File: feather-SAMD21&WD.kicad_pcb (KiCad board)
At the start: 2 copper layers, 50.8 x 22.9 mm, 35 parts, among them J1 JumperSET0, J2 JumperSET1, J3 JumperSET2, J4 left_header, J5 right_header, J6 Batt_header, J7 reset_enable, J8 16P_USB_C, SW1 SW_Push, U1 MAX6369, U2 USBLC6-2SC6, U3 ATSAMD21G18A-M, X1 32.768

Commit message: rev one, routing done
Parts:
- moved R5 8.13 mm to (140.4, 88.4)
- moved SW1 1.50 mm to (138.4, 86.6)
- moved C2 1.46 mm to (146.0, 85.0)
- moved C1 0.89 mm to (140.4, 92.4), turned to 180 degrees
- moved R4 0.89 mm to (140.4, 90.4), turned to 180 degrees
- moved U1 0.59 mm to (145.9, 88.2)
- moved C4 0.54 mm to (136.8, 86.4)
- moved U2 0.52 mm to (117.4, 86.3)
- moved C6 0.51 mm to (131.5, 91.7), turned to 0 degrees
- moved C9 0.50 mm to (124.2, 84.4)
- moved C3 0.43 mm to (127.4, 79.1)
- moved C5 0.40 mm to (124.6, 88.2)
- moved D1 0.40 mm to (122.2, 87.9)
- moved R8 0.40 mm to (122.2, 84.3)
- moved X1 0.35 mm to (127.2, 91.7)
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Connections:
- U1 pad 1: A0 -> D1
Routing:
- net +3.3V: track 0.00 -> 150.9 mm, vias 0 -> 6
- net ~{RESET}: track 0.89 -> 94.2 mm, vias 0 -> 3
- net GND: track 0.00 -> 50.0 mm, vias 0 -> 25
- net D1: track 0.00 -> 34.5 mm, vias 0 -> 1
- net VBUS: track 0.00 -> 30.2 mm
- net SDA: track 0.00 -> 24.5 mm, vias 0 -> 1
- net SCL: track 0.00 -> 23.7 mm, vias 0 -> 1
- net D13: track 0.00 -> 21.1 mm, vias 0 -> 2
- net MISO: track 0.00 -> 20.8 mm, vias 0 -> 1
- net D0: track 0.00 -> 19.6 mm
- net D9: track 0.76 -> 19.1 mm, vias 0 -> 2
- net D6: track 0.00 -> 18.1 mm, vias 0 -> 1
- net MOSI: track 0.00 -> 18.1 mm, vias 0 -> 1
- net D5: track 0.51 -> 17.6 mm
- net D-: track 0.00 -> 16.8 mm
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- added copper zone on B.Cu, net GND
- added copper zone on F.Cu, net GND
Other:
- board size 50.8 x 22.9 mm -> 51.6 x 24.1 mm

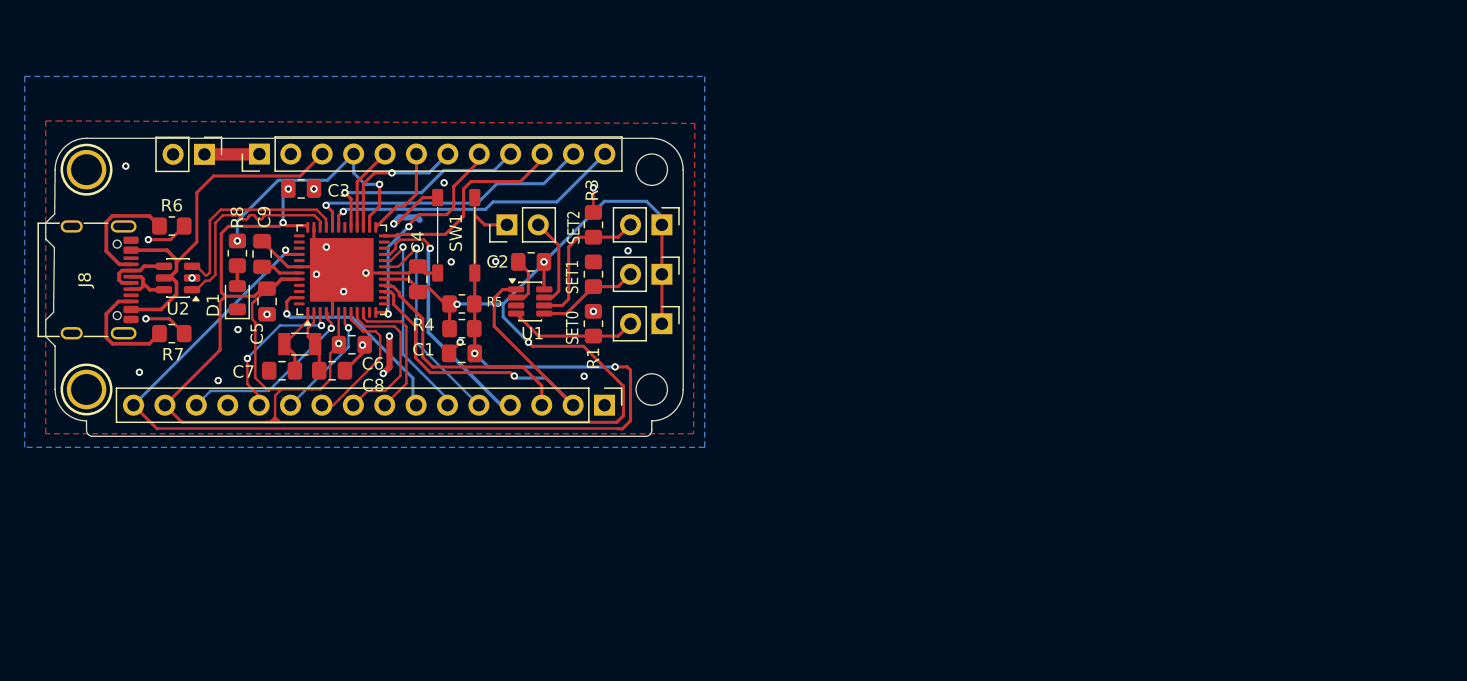
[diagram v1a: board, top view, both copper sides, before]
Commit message: V3 schematic updated
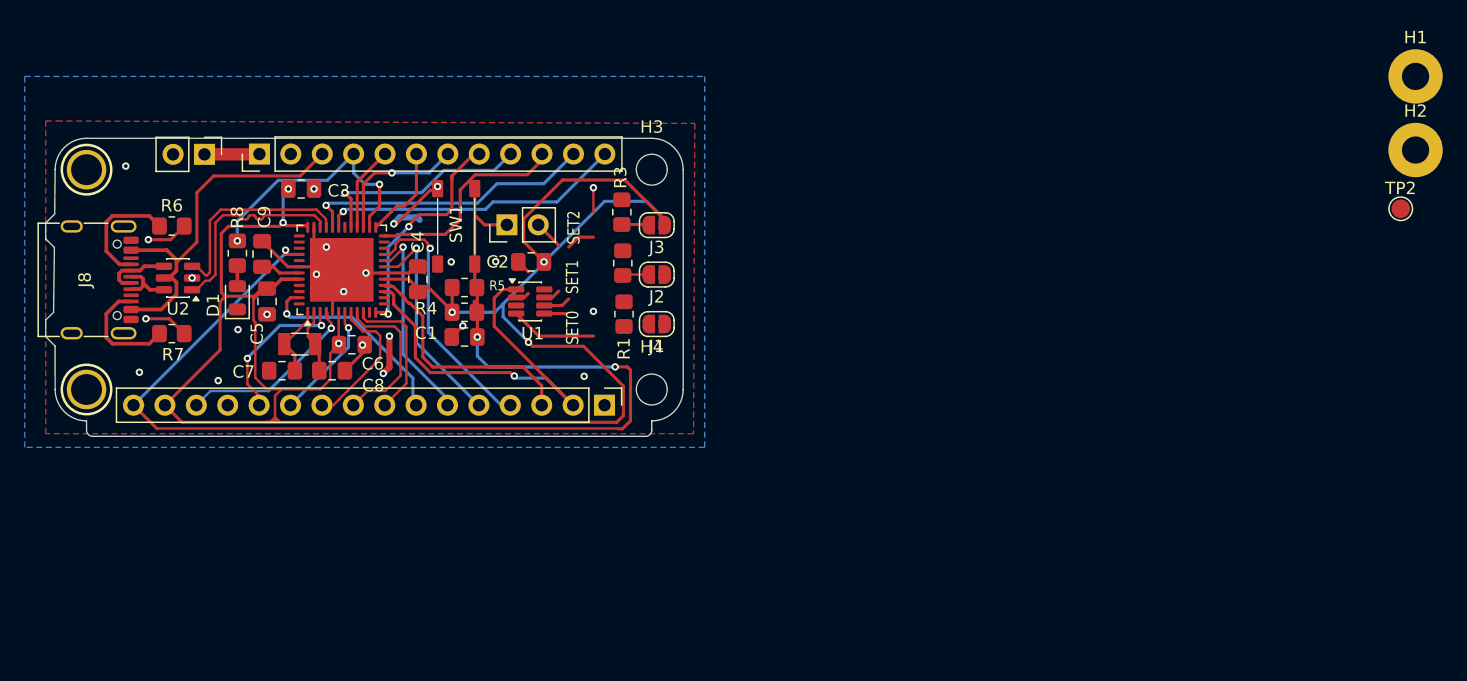
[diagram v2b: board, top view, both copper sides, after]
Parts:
- removed UNK_HOLE_0: , dummyfp0
- removed UNK_HOLE_1: , dummyfp1
- added H1: MountingHole_Pad, MountingHole:MountingHole_2.2mm_M2_Pad, F.Cu at (217.5, 70.0)
- added H2: MountingHole_Pad, MountingHole:MountingHole_2.2mm_M2_Pad, F.Cu at (217.5, 76.0)
- added H3: MountingHole, MountingHole:MountingHole_2.5mm, F.Cu at (155.7, 77.5)
- added H4: MountingHole, MountingHole:MountingHole_2.5mm, F.Cu at (155.7, 95.3)
- added TP2: TestPoint_Small, TestPoint:TestPoint_Pad_D1.5mm, F.Cu at (216.3, 80.7)
- J1, J2, J3: footprint Connector_PinHeader_2.54mm:PinHeader_1x02_P2.54mm_Vertical -> Jumper:SolderJumper-2_P1.3mm_Open_RoundedPad1.0x1.5mm
- moved R1 2.59 mm to (153.5, 89.2)
- moved R2 2.54 mm to (153.4, 85.1)
- moved R3 2.52 mm to (153.3, 81.0)
- moved C1 1.34 mm to (140.6, 91.1)
- moved R4 1.34 mm to (140.6, 89.1)
- moved R5 1.34 mm to (140.6, 87.1)
- moved SW1 0.72 mm to (138.4, 85.9)
- moved J1 0.42 mm to (156.1, 90.0), turned to 180 degrees
- moved J2 0.42 mm to (156.1, 86.0), turned to 180 degrees
- moved J3 0.42 mm to (156.1, 82.0), turned to 180 degrees
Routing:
- net +3.3V: track 150.9 -> 161.4 mm
- net SET2: track 12.1 -> 6.52 mm
- net SET1: track 8.29 -> 3.93 mm
- net Net-(J7-Pin_2): track 7.43 -> 3.74 mm
- net SET0: track 10.4 -> 7.01 mm
- net GND: track 50.0 -> 47.6 mm, vias 25 -> 24
- net ~{RESET}: track 94.2 -> 95.5 mm

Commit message: v3 layout done
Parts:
- removed TP2: TestPoint_Small, TestPoint:TestPoint_Pad_D1.5mm
- removed U$31, U$32: MOUNTINGHOLE2.5, MOUNTINGHOLE_2.5_PLATED
- added 555: LM555xMM, Package_SO:VSSOP-8_3x3mm_P0.65mm, F.Cu at (125.7, 89.5)
- added C10: 22u, Capacitor_SMD:C_0805_2012Metric_Pad1.18x1.45mm_HandSolder, F.Cu at (120.9, 82.9)
- added C11: 22u, Capacitor_SMD:C_0805_2012Metric_Pad1.18x1.45mm_HandSolder, F.Cu at (120.9, 85.5)
- added C12: C, Capacitor_SMD:C_0805_2012Metric_Pad1.18x1.45mm_HandSolder, F.Cu at (122.5, 92.8)
- added C13: 10n, Capacitor_SMD:C_0805_2012Metric_Pad1.18x1.45mm_HandSolder, F.Cu at (127.0, 92.8)
- added D2: LED, LED_SMD:LED_0805_2012Metric_Pad1.15x1.40mm_HandSolder, F.Cu at (149.1, 91.9)
- added D3: D_Schottky, Diode_SMD:D_SOD-123, F.Cu at (114.0, 77.4)
- added D4: LED, LED_SMD:LED_0805_2012Metric, F.Cu at (113.6, 81.6)
- added J10: monostable bypass jumper, Jumper:SolderJumper-2_P1.3mm_Open_Pad1.0x1.5mm, B.Cu at (122.6, 86.6)
- added J9: wd_pwr_jumper, Jumper:SolderJumper-2_P1.3mm_Open_RoundedPad1.0x1.5mm, B.Cu at (126.0, 87.2)
- added R10: 2k2, Resistor_SMD:R_0805_2012Metric_Pad1.20x1.40mm_HandSolder, F.Cu at (149.1, 89.9)
- added R11: 100k, Resistor_SMD:R_0805_2012Metric_Pad1.20x1.40mm_HandSolder, F.Cu at (127.7, 81.3)
- added R12: 100k, Resistor_SMD:R_0805_2012Metric_Pad1.20x1.40mm_HandSolder, F.Cu at (127.7, 83.5)
- added R13: Rprog, Resistor_SMD:R_0805_2012Metric_Pad1.20x1.40mm_HandSolder, F.Cu at (124.4, 80.8)
- added R14: 2k2, Resistor_SMD:R_0805_2012Metric_Pad1.20x1.40mm_HandSolder, F.Cu at (138.9, 92.5)
- added R15: 2k2, Resistor_SMD:R_0805_2012Metric_Pad1.20x1.40mm_HandSolder, F.Cu at (127.7, 79.1)
- added R16: R, Resistor_SMD:R_0805_2012Metric_Pad1.20x1.40mm_HandSolder, F.Cu at (129.8, 88.9)
- added R9: 2k2, Resistor_SMD:R_0805_2012Metric_Pad1.20x1.40mm_HandSolder, F.Cu at (116.8, 81.2)
- added U4: AP2112K-3.3, Package_TO_SOT_SMD:SOT-23-5, F.Cu at (116.7, 84.5)
- added U5: MCP73832-2-OT, Package_TO_SOT_SMD:SOT-23-5, F.Cu at (121.1, 79.8)
- added U6: AP2112K-3.3, Package_TO_SOT_SMD:SOT-23-5, F.Cu at (132.1, 92.8)
- added μcLED: LED, LED_SMD:LED_0805_2012Metric_Pad1.15x1.40mm_HandSolder, F.Cu at (141.7, 92.8)
- C6: value 100n -> 22pf
- C8: value 22pf -> 1u
- C9: value 1u -> 4.7u
- H1, H2: footprint MountingHole:MountingHole_2.2mm_M2_Pad -> Library:feather_mounting hole M2.5
- H3, H4: footprint MountingHole:MountingHole_2.5mm -> Library:feather_mounting hole (no pad)
- J1, J2, J3: moved to B.Cu
- J7: footprint Connector_PinHeader_2.54mm:PinHeader_1x02_P2.54mm_Vertical -> Jumper:SolderJumper-2_P1.3mm_Open_RoundedPad1.0x1.5mm; moved to B.Cu
- moved H2 109.2 mm to (110.0, 95.3)
- moved H1 107.8 mm to (110.0, 77.5)
- moved J8 45.9 mm to (155.8, 86.4), turned to 90 degrees
- moved J1 43.6 mm to (112.6, 87.4), turned to -90 degrees
- moved J2 40.6 mm to (115.6, 87.3), turned to -90 degrees
- moved R1 40.4 mm to (113.1, 91.5), turned to -90 degrees
- moved R6 38.4 mm to (153.8, 92.8), turned to 180 degrees
- moved R7 38.1 mm to (153.4, 80.0), turned to 180 degrees
- moved J3 37.9 mm to (118.6, 87.3), turned to -90 degrees
- moved R3 37.7 mm to (116.2, 87.5), turned to 180 degrees
- moved R2 36.5 mm to (117.7, 93.0), turned to 180 degrees
- moved C1 32.1 mm to (110.0, 81.2)
- moved U2 31.5 mm to (148.9, 85.1)
- moved R4 30.8 mm to (109.9, 91.2)
- moved SW1 30.2 mm to (108.5, 89.9)
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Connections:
- C2 pad 1: +3.3V -> +3.3Vwd
- C3 pad 1: +3.3V -> +3.3Vmcu
- C4 pad 1: +3.3V -> +3.3Vmcu
- C5 pad 1: +3.3V -> +3.3Vmcu
- C6 pad 1: +3.3V -> GND
- C6 pad 2: GND -> Net-(U3-PA00)
- C7 pad 1: GND -> Net-(U3-PA01)
- C7 pad 2: Net-(U3-PA00) -> GND
- C8 pad 1: Net-(U3-PA01) -> GND
- C8 pad 2: GND -> Net-(U3-VDDCORE)
- C9 pad 1: GND -> +BATT
- C9 pad 2: Net-(U3-VDDCORE) -> GND
- J1 pad 1: +3.3V -> +3.3Vsys
- J2 pad 1: +3.3V -> +3.3Vsys
- J3 pad 1: +3.3V -> +3.3Vsys
- J4 pad 15: +3.3V -> +3.3Vsys
- J7 pad 1: ~{RESET} -> WDO
- R4 pad 2: +3.3V -> +3.3Vsys
- R5 pad 1: +3.3V -> +3.3Vwd
- R5 pad 2: ~{RESET} -> WDO
- U1 pad 1: D1 -> A0
- U1 pad 8: +3.3V -> +3.3Vwd
- U3 pad 17: +3.3V -> +3.3Vmcu
- U3 pad 36: +3.3V -> +3.3Vmcu
- U3 pad 39: TXLED -> ldoEN
- U3 pad 44: +3.3V -> +3.3Vmcu
- U3 pad 48: RXLED -> batt_ADC
- U3 pad 6: +3.3V -> +3.3Vmcu
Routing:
- net +3.3V: track 161.4 -> 0.00 mm, vias 6 -> 0
- net ~{RESET}: track 95.5 -> 0.00 mm, vias 3 -> 0
- net D1: track 34.5 -> 0.00 mm, vias 1 -> 0
- net GND: track 47.6 -> 15.2 mm, vias 24 -> 0
- net VBUS: track 30.2 -> 0.00 mm
- net SDA: track 24.5 -> 0.00 mm, vias 1 -> 0
- net SCL: track 23.7 -> 0.00 mm, vias 1 -> 0
- net D13: track 21.1 -> 0.00 mm, vias 2 -> 0
- net MISO: track 20.8 -> 0.00 mm, vias 1 -> 0
- net D0: track 19.7 -> 0.00 mm
- net D9: track 19.4 -> 0.00 mm, vias 2 -> 0
- net MOSI: track 18.1 -> 0.00 mm, vias 1 -> 0
- net D6: track 18.1 -> 0.38 mm, vias 1 -> 0
- net D5: track 17.7 -> 0.00 mm
- net D-: track 16.8 -> 0.00 mm
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- added copper zone on In1.Cu, net (none)
- added copper zone on In2.Cu, net +3.3Vmcu
- added copper zone on In2.Cu, net +3.3Vsys
- removed copper zone on B.Cu, net GND
- removed copper zone on F.Cu, net GND
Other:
- board size 51.6 x 24.1 mm -> 51.6 x 22.9 mm
- copper layers 2 -> 4
- board text added: "3.3"
- board text added: "3.3sysLED"
- board text added: "Charger LED >"
- board text added: "D13LED"
- board text added: "J10 - latch Bypass"
- board text added: "J7 - wdo en"
- board text added: "J9 - wd pwr en"
- board text added: "LDO"
- board text added: "S0"
- board text added: "S1"
- board text added: "S2"
- board text removed: "SET0"
- board text removed: "SET1"
- board text removed: "SET2"

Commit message: final changes, everythings done
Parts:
- added 3.3wd: TestPoint_Small, TestPoint:TestPoint_Pad_D1.5mm, B.Cu at (155.9, 84.8)
- added 3.3μC: TestPoint_Small, TestPoint:TestPoint_Pad_D1.5mm, B.Cu at (126.8, 89.6)
- added BattADC: TestPoint_Small, TestPoint:TestPoint_Pad_D1.5mm, B.Cu at (122.8, 89.6)
- added Disch: TestPoint_Small, TestPoint:TestPoint_Pad_D1.5mm, B.Cu at (149.7, 80.4)
- added G***: LOGO, LOGO, F.Cu at (119.8, 110.1)
- added G***: LOGO, LOGO, F.Cu at (120.0, 110.8)
- added G***: LOGO, LOGO, B.Cu at (100.8, 106.5)
- added G***: LOGO, LOGO, B.Cu at (116.6, 87.1)
- added LdoEN: TestPoint_Small, TestPoint:TestPoint_Pad_D1.5mm, B.Cu at (127.0, 82.8)
- added RESET: TestPoint_Small, TestPoint:TestPoint_Pad_D1.5mm, B.Cu at (126.8, 86.0)
- added Thresh: TestPoint_Small, TestPoint:TestPoint_Pad_D1.5mm, B.Cu at (150.1, 83.0)
- added WDO: TestPoint_Small, TestPoint:TestPoint_Pad_D1.5mm, B.Cu at (147.6, 83.6)
- J4, J5: moved to B.Cu
- moved SW1 49.3 mm to (157.5, 85.2), turned to -90 degrees
- moved R4 46.8 mm to (155.6, 81.1), turned to 0 degrees
- moved J8 45.9 mm to (109.9, 86.4), turned to -90 degrees
- moved C1 45.7 mm to (155.7, 83.2), turned to 0 degrees
- moved R6 42.1 mm to (113.7, 80.1), turned to 0 degrees
- moved R7 41.5 mm to (113.9, 92.8), turned to 0 degrees
- moved R3 36.7 mm to (152.7, 90.7), turned to -90 degrees
- moved J3 34.4 mm to (152.9, 89.2)
- moved J2 33.9 mm to (149.4, 89.2)
- moved J1 33.4 mm to (145.9, 89.2), turned to 90 degrees
- moved WD 33.2 mm to (149.5, 88.9)
- moved R1 32.0 mm to (145.0, 88.2), turned to 180 degrees
- moved R2 31.9 mm to (149.6, 91.6)
- moved U2 31.8 mm to (117.0, 85.7)
- moved C12 29.5 mm to (151.0, 85.0), turned to -90 degrees
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- renumbered μcLED to McuLED, U1 to WD
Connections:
- WD pad 1: A0 -> D1
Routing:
- net GND: track 15.2 -> 100.9 mm, vias 0 -> 20
- net ~{RESET}: track 0.00 -> 60.6 mm, vias 0 -> 2
- net +3.3Vwd: track 0.00 -> 33.0 mm, vias 0 -> 1
- net VBUS: track 0.00 -> 32.4 mm, vias 0 -> 1
- net D1: track 0.00 -> 28.0 mm
- net +BATT: track 6.70 -> 33.3 mm, vias 0 -> 2
- net SDA: track 0.00 -> 23.5 mm, vias 0 -> 2
- net SCL: track 0.00 -> 23.4 mm, vias 0 -> 2
- net ldoEN: track 0.00 -> 23.3 mm, vias 0 -> 3
- net EN: track 0.00 -> 23.3 mm, vias 0 -> 1
- net D9: track 0.00 -> 19.4 mm, vias 0 -> 3
- net D6: track 0.38 -> 18.6 mm, vias 0 -> 2
- net D0: track 0.00 -> 17.4 mm, vias 0 -> 1
- net AREF: track 0.00 -> 16.3 mm, vias 0 -> 1
- net D+: track 0.00 -> 16.2 mm
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- added copper zone on B.Cu, net GND
- added copper zone on F.Cu, net GND
- added copper zone on In1.Cu, net GND
- removed copper zone on In1.Cu, net (none)
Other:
- outline, holes or cut-outs redrawn
- board text added: "+BATT"
- board text added: "-BATT"
- board text added: "10~~"
- board text added: "11~~"
- board text added: "12"
- board text added: "13"
- board text added: "3V3"
- board text added: "5"
- board text added: "59 4F 47 20 57 4D 4B 43"
- board text added: "6"
- board text added: "9~~"
- board text added: "A0"
- board text added: "A1"
- board text added: "A2"
- board text added: "A3"
- board text added: "A4"
- board text added: "A5"
- board text added: "Aref"
- board text added: "BAT"
- board text added: "ChargerLED"
- board text added: "D0"
- board text added: "D1"
- board text added: "En"
- board text added: "GND"
- board text added: "J9 - wd pwr en J7 - wdo en J10 - latch Bypass"
- board text added: "MISO"
- board text added: "MOSI"
- board text added: "RST"
- board text added: "SAMD21G18A + MAX63XX watchdog dev board"
- board text added: "SCK"
- board text added: "SCL"
- board text added: "SDA"
- board text added: "SysLED"
- board text added: "USB"
- board text added: "~~"
- board text removed: "3.3sysLED"
- board text removed: "Charger LED >"
- board text removed: "J10 - latch Bypass"
- board text removed: "J7 - wdo en"
- board text removed: "J9 - wd pwr en"
